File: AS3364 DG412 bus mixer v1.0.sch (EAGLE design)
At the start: 118 parts, among them IC1 PCA9539PW, IC10 DG412-J, IC11 DG412-J, IC14 TL074JT, IC2 TL074JT, IC3 TL072JT, IC4 TL074JT, IC6 TL072JT, IC8 DG412-J, IC9 DG412-J

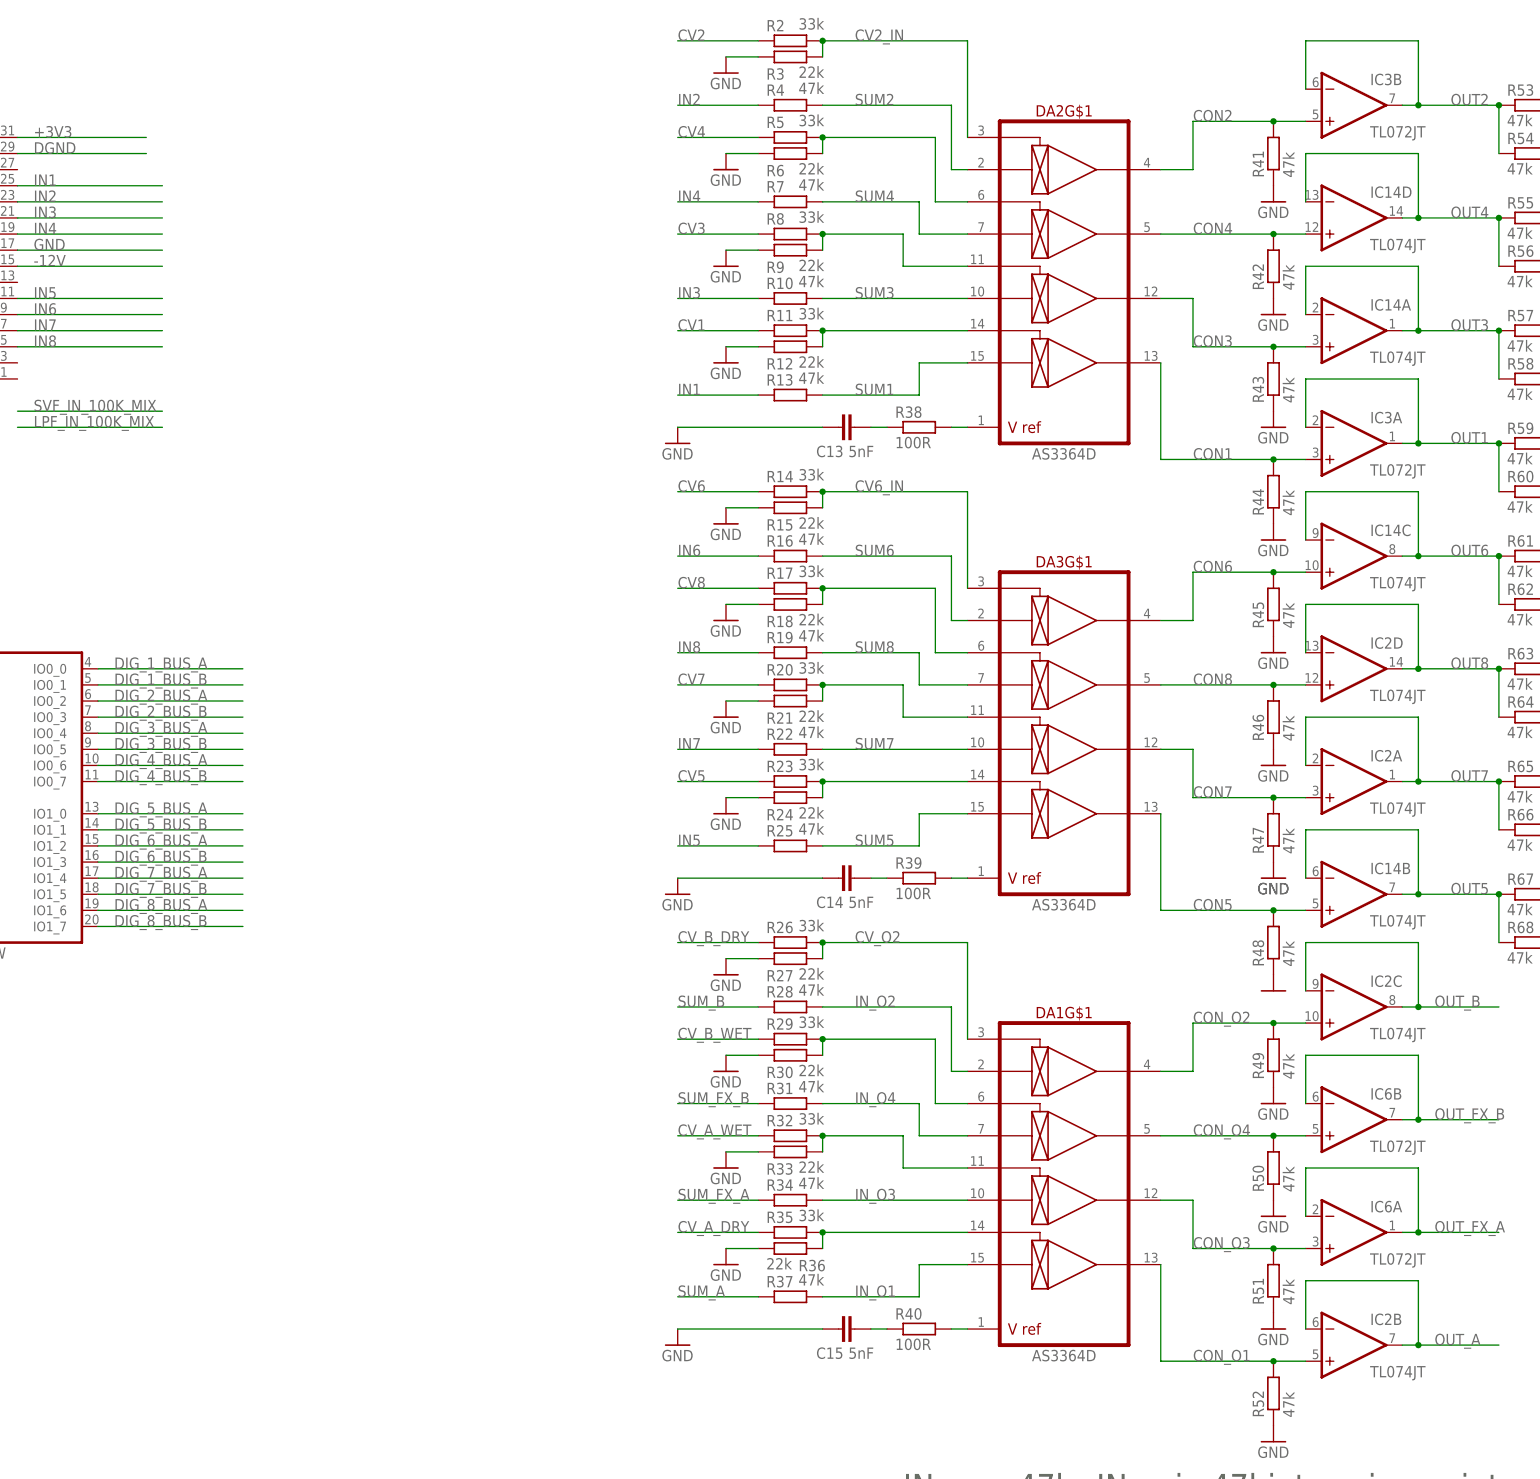
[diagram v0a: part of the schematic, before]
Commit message: Finished tracing switches and vcas internally
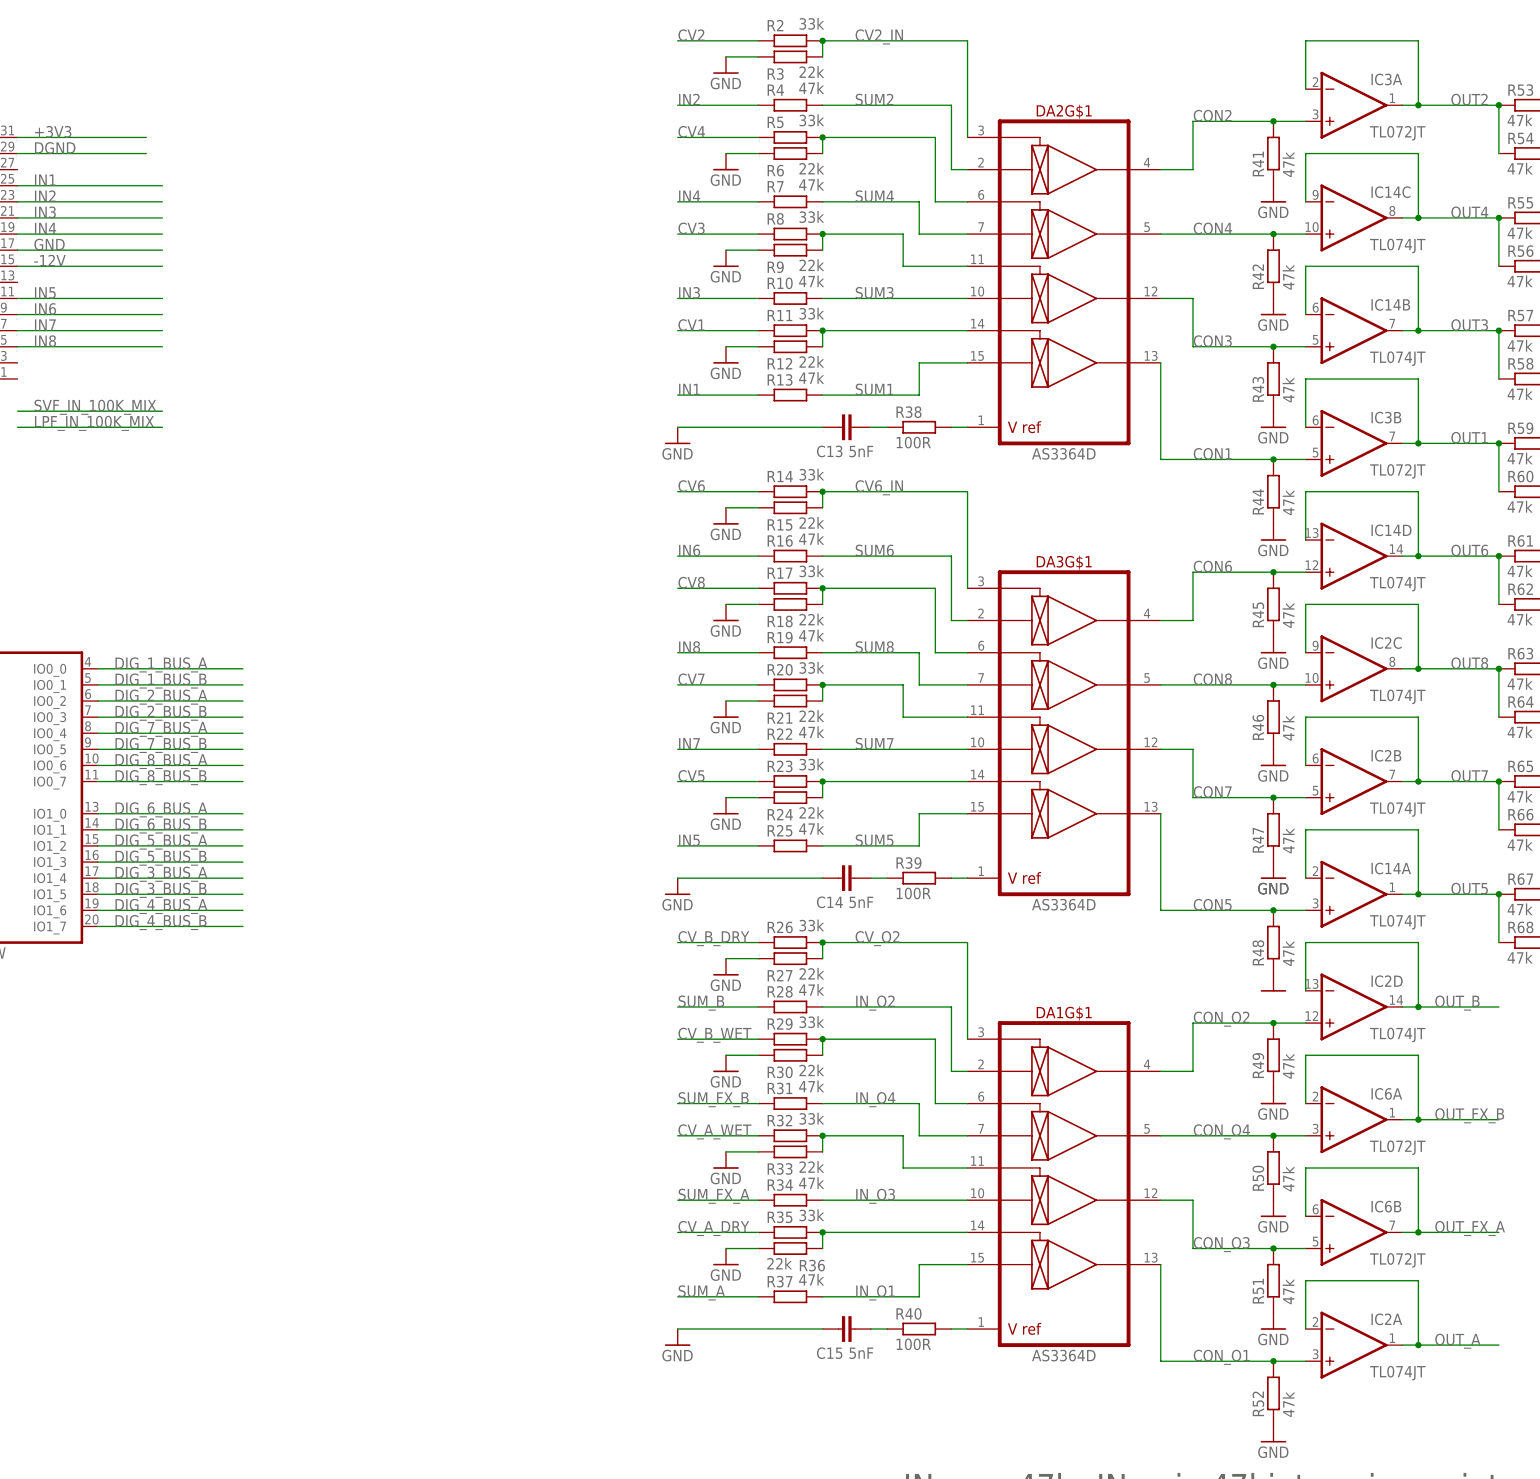
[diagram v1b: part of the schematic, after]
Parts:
- R77, R78: device rcl:R-EU_R0603 -> rcl:R-EU_R0402
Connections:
- net CON1: now also IC3B.+IN; no longer IC3A.+IN
- net CON2: now also IC3A.+IN; no longer IC3B.+IN
- net CON3: now also IC14B.+IN; no longer IC14A.+IN
- net CON4: now also IC14C.+IN; no longer IC14D.+IN
- net CON5: now also IC14A.+IN; no longer IC14B.+IN
- net CON6: now also IC14D.+IN; no longer IC14C.+IN
- net CON7: now also IC2B.+IN; no longer IC2A.+IN
- net CON8: now also IC2C.+IN; no longer IC2D.+IN
- net CON_O1: now also IC2A.+IN; no longer IC2B.+IN
- net CON_O2: now also IC2D.+IN; no longer IC2C.+IN
- net CON_O3: now also IC6B.+IN; no longer IC6A.+IN
- net CON_O4: now also IC6A.+IN; no longer IC6B.+IN
- net DIG_3_BUS_A: now also IC1.IO1_4; no longer IC1.IO0_4
- net DIG_3_BUS_B: now also IC1.IO1_5; no longer IC1.IO0_5
- net DIG_4_BUS_A: now also IC1.IO1_6; no longer IC1.IO0_6
- net DIG_4_BUS_B: now also IC1.IO1_7; no longer IC1.IO0_7
- net DIG_5_BUS_A: now also IC1.IO1_2; no longer IC1.IO1_0
- net DIG_5_BUS_B: now also IC1.IO1_3; no longer IC1.IO1_1
- net DIG_6_BUS_A: now also IC1.IO1_0; no longer IC1.IO1_2
- net DIG_6_BUS_B: now also IC1.IO1_1; no longer IC1.IO1_3
- net DIG_7_BUS_A: now also IC1.IO0_4; no longer IC1.IO1_4
- net DIG_7_BUS_B: now also IC1.IO0_5; no longer IC1.IO1_5
- net DIG_8_BUS_A: now also IC1.IO0_6; no longer IC1.IO1_6
- net DIG_8_BUS_B: now also IC1.IO0_7; no longer IC1.IO1_7
- net OUT1: now also IC3B.-IN, IC3B.OUT; no longer IC3A.-IN, IC3A.OUT
- net OUT2: now also IC3A.-IN, IC3A.OUT; no longer IC3B.-IN, IC3B.OUT
- net OUT3: now also IC14B.-IN, IC14B.OUT; no longer IC14A.-IN, IC14A.OUT
- net OUT4: now also IC14C.-IN, IC14C.OUT; no longer IC14D.-IN, IC14D.OUT
- net OUT5: now also IC14A.-IN, IC14A.OUT; no longer IC14B.-IN, IC14B.OUT
- net OUT6: now also IC14D.-IN, IC14D.OUT; no longer IC14C.-IN, IC14C.OUT
- net OUT7: now also IC2B.-IN, IC2B.OUT; no longer IC2A.-IN, IC2A.OUT
- net OUT8: now also IC2C.-IN, IC2C.OUT; no longer IC2D.-IN, IC2D.OUT
- net OUT_A: now also IC2A.-IN, IC2A.OUT; no longer IC2B.-IN, IC2B.OUT
- net OUT_B: now also IC2D.-IN, IC2D.OUT; no longer IC2C.-IN, IC2C.OUT
- net OUT_FX_A: now also IC6B.-IN, IC6B.OUT; no longer IC6A.-IN, IC6A.OUT
- net OUT_FX_B: now also IC6A.-IN, IC6A.OUT; no longer IC6B.-IN, IC6B.OUT
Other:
- moved on the sheet: IC14A, IC14B, IC14C, IC14D, IC2A, IC2B, IC2C, IC2D, IC3A, IC3B, IC6A, IC6B

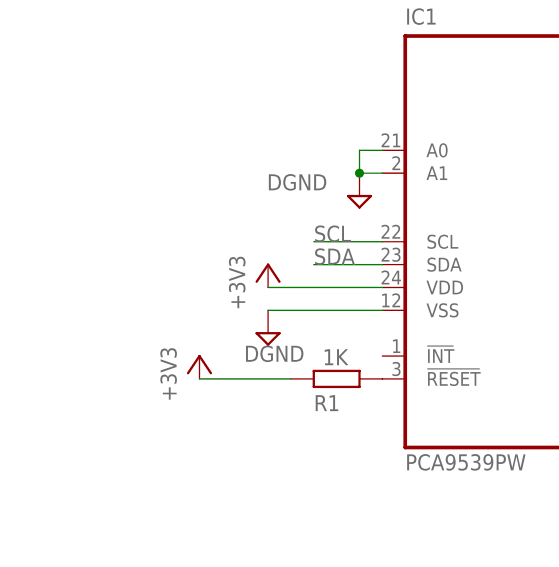
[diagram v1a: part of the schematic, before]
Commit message: Digital lines traced
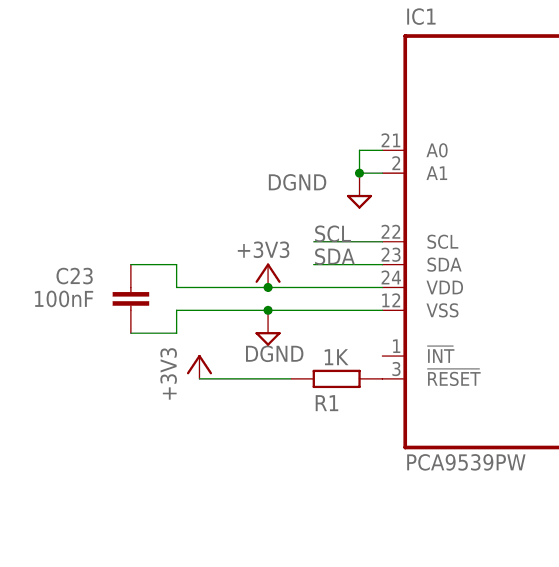
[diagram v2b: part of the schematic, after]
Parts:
- added C23: 100nF, rcl:C-EUC0402
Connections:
- net +3V3: now also C23.2
- net DGND: now also C23.1
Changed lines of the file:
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@@
 <part name="IC2" library="joakim" deviceset="TL074J" device="T"/>
 <part name="IC4" library="joakim" deviceset="TL074J" device="T"/>
+<part name="C23" library="rcl" library_urn="urn:adsk.eagle:library:334" deviceset="C-EU" device="C0402" package3d_urn="urn:adsk.eagle:package:23626/2" value="100nF"/>
 </parts>
 <sheets>
@@
 </instance>
 <instance part="+3V17" gate="G$1" x="-167.64" y="-27.94" smashed="yes">
-<attribute name="VALUE" x="-170.18" y="-33.02" size="1.778" layer="96" rot="R90"/>
+<attribute name="VALUE" x="-165.1" y="-25.4" size="1.778" layer="96" rot="R180"/>
 </instance>
 <instance part="SUPPLY30" gate="G$1" x="-157.48" y="-20.32" smashed="yes">
@@
 <attribute name="NAME" x="76.2" y="-55.245" size="1.778" layer="95"/>
 <attribute name="VALUE" x="76.2" y="-63.5" size="1.778" layer="96"/>
+</instance>
+<instance part="C23" gate="G$1" x="-182.88" y="-33.02" smashed="yes" rot="R180">
+<attribute name="NAME" x="-186.944" y="-28.321" size="1.778" layer="95" rot="R180"/>
+<attribute name="VALUE" x="-186.944" y="-30.861" size="1.778" layer="96" rot="R180"/>
 </instance>
 </instances>
@@
 <wire x1="-154.94" y1="-30.48" x2="-167.64" y2="-30.48" width="0.1524" layer="91"/>
 <pinref part="+3V17" gate="G$1" pin="+3V3"/>
+<wire x1="-167.64" y1="-30.48" x2="-177.8" y2="-30.48" width="0.1524" layer="91"/>
+<junction x="-167.64" y="-30.48"/>
+<wire x1="-177.8" y1="-30.48" x2="-177.8" y2="-27.94" width="0.1524" layer="91"/>
+<pinref part="C23" gate="G$1" pin="2"/>
+<wire x1="-177.8" y1="-27.94" x2="-182.88" y2="-27.94" width="0.1524" layer="91"/>
 </segment>
 <segment>
@@
 <pinref part="SUPPLY21" gate="G$1" pin="DGND"/>
 <wire x1="-154.94" y1="-33.02" x2="-167.64" y2="-33.02" width="0.1524" layer="91"/>
-</segment>
-<segment>
+<wire x1="-167.64" y1="-33.02" x2="-177.8" y2="-33.02" width="0.1524" layer="91"/>
+<junction x="-167.64" y="-33.02"/>
+<wire x1="-177.8" y1="-33.02" x2="-177.8" y2="-35.56" width="0.1524" layer="91"/>
+<pinref part="C23" gate="G$1" pin="1"/>
+<wire x1="-177.8" y1="-35.56" x2="-182.88" y2="-35.56" width="0.1524" layer="91"/>
+</segment>
+<segment>
